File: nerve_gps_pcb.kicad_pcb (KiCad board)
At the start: 4 copper layers, 50 x 50 mm, 14 parts, among them J1 BF080-16-A-1-L-C, J2 WS2812B, J3 5V GPIO Breakout, U1 SAM-M10Q, U2 TXB0104QPWRQ1

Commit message: Update config.kibot.yaml, cleanup, add fiducials
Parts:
- added FM1: 1mm, Fiducial:Fiducial_1mm_Mask2mm, F.Cu at (129.8, 120.0)
- added FM2: 1mm, Fiducial:Fiducial_1mm_Mask2mm, F.Cu at (129.8, 90.0)
- added FM3: 1mm, Fiducial:Fiducial_1mm_Mask2mm, F.Cu at (167.2, 90.0)
- added FM4: 1mm, Fiducial:Fiducial_1mm_Mask2mm, B.Cu at (129.8, 120.0)
- added FM5: 1mm, Fiducial:Fiducial_1mm_Mask2mm, B.Cu at (129.8, 90.0)
- added FM6: 1mm, Fiducial:Fiducial_1mm_Mask2mm, B.Cu at (167.2, 90.0)
- turned H2 to 135 degrees
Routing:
- net Net-(D4-DOUT): track 14.9 -> 16.3 mm

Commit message: Major cleanup and update component_library
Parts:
- U2: moved to B.Cu
- moved J3 20.5 mm to (171.0, 102.5), turned to 180 degrees
- moved J2 11.9 mm to (159.7, 89.5), turned to 90 degrees
- moved U2 7.98 mm to (161.5, 105.0)
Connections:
- net +3.3VBATT renamed +3VBATT
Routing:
- net /GPIO_3_{5V}: track 28.7 -> 13.2 mm
- net +3V3: track 38.8 -> 25.5 mm, vias 10 -> 4
- net /GPIO_2_{5V}: track 24.5 -> 11.5 mm
- net /GPIO_1_{5V}: track 20.3 -> 9.66 mm
- net Net-(D4-DOUT): track 16.3 -> 8.76 mm
- net GND: track 45.1 -> 41.0 mm, vias 92 -> 111
- net /GPIO_3: track 12.5 -> 9.01 mm, vias 1 -> 0
- net /GPIO_2: track 10.1 -> 7.18 mm, vias 1 -> 0
- net /GPIO_1: track 6.47 -> 5.49 mm, vias 1 -> 0
- net /GPS_UART_RX: track 20.4 -> 19.5 mm
- net +3VBATT: track 52.5 -> 51.8 mm
- net /GPS_UART_TX: track 20.2 -> 19.5 mm
- net +5V: track 12.7 -> 13.1 mm, vias 5 -> 8
- added copper zone on F.Cu, net +5V
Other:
- board text added: "5V"
- board text added: "CR1220 3V"
- board text added: "GND"
- board text added: "GPIO1_{5V}"
- board text added: "GPIO2_{5V}"
- board text added: "GPIO3_{5V}"
- board text added: "PWM_{RGB}"

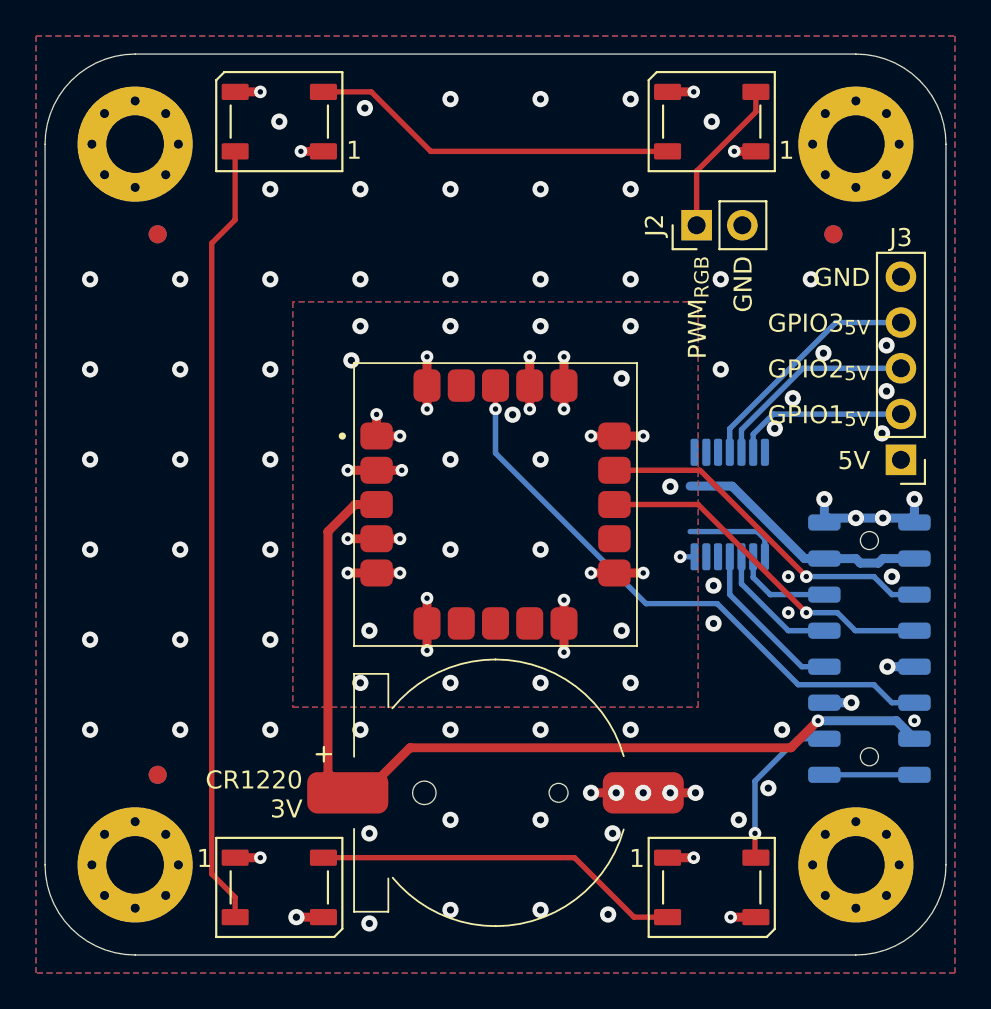
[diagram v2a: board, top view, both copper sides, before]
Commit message: Cleanup silkscreen
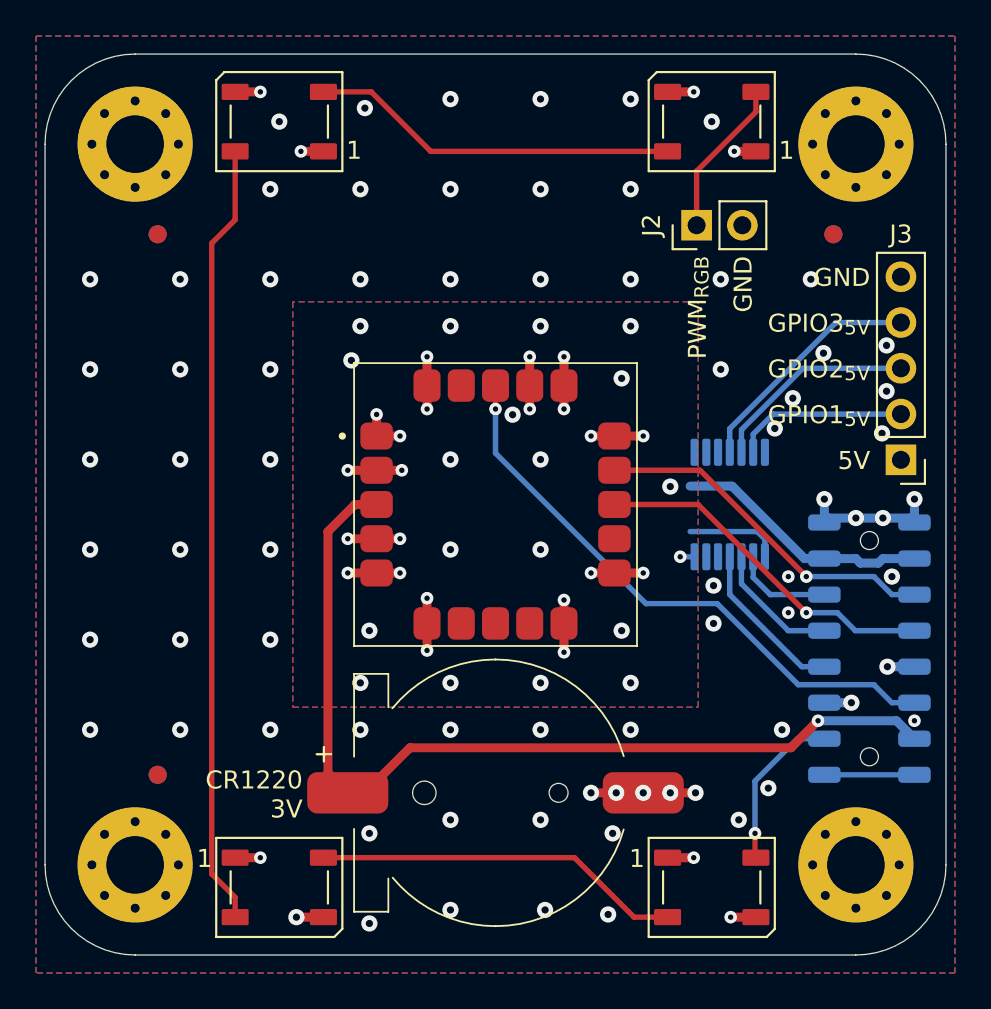
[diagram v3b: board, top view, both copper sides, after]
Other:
- board text added: "Daniel Jeon nerve_gps_pcb v0.1.0-alpha"
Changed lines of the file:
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@@
 		(tags "Through hole pin header THT 1x02 2.54mm single row")
 		(property "Reference" "J2"
-			(at 0 -2.33 90)
+			(at 0 -2.5 90)
 			(layer "F.SilkS")
 			(effects
@@
 		(tags "Through hole pin header THT 1x05 2.54mm single row")
 		(property "Reference" "J3"
-			(at 0 12.325 180)
+			(at 0 12.52 180)
 			(layer "F.SilkS")
 			(effects
@@
 				(font
 					(size 1 1)
-					(thickness 0.1)
+					(thickness 0.15)
 				)
 				(justify mirror)
@@
 		)
 	)
+	(gr_text "Daniel Jeon\nnerve_gps_pcb\nv0.1.0-alpha"
+		(at 148.5 128.75 0)
+		(layer "B.SilkS")
+		(effects
+			(font
+				(size 1 1)
+				(thickness 0.2)
+				(bold yes)
+			)
+			(justify bottom mirror)
+		)
+	)
 	(gr_text "GPIO3_{5V}"
 		(at 169.32619 95.53 0)
@@
 	)
 	(via
-		(at 151 127.5)
+		(at 151.25 127.5)
 		(size 0.9)
 		(drill 0.4)

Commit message: Fix #2
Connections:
- U1 pad 13: /GPS_UART_RX -> /GPS_UART_TX
- U1 pad 14: /GPS_UART_TX -> /GPS_UART_RX
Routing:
- net /GPS_UART_RX: track 19.5 -> 20.3 mm
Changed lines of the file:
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@@
 			(layers "F.Cu" "F.Mask")
 			(roundrect_rratio 0.25)
-			(net 11 "/GPS_UART_RX")
+			(net 8 "/GPS_UART_TX")
 			(pinfunction "TXD")
 			(pintype "output")
@@
 			(layers "F.Cu" "F.Mask")
 			(roundrect_rratio 0.25)
-			(net 8 "/GPS_UART_TX")
+			(net 11 "/GPS_UART_RX")
 			(pinfunction "RXD")
 			(pintype "input")
@@
 	)
 	(via
-		(at 164.75 109)
+		(at 164.849997 109)
 		(size 0.7)
 		(drill 0.3)
@@
 	)
 	(via
-		(at 158.200216 104.001988)
+		(at 157 104.001988)
 		(size 0.9)
 		(drill 0.4)
@@
 	)
 	(segment
-		(start 165.75 109)
-		(end 159.85 103.1)
+		(start 165.75 111)
+		(end 159.75 105)
 		(width 0.3)
 		(layer "F.Cu")
@@
 	)
 	(segment
-		(start 159.85 103.1)
-		(end 155.1 103.1)
+		(start 169.25 111)
+		(end 165.75 111)
+		(width 0.3)
+		(layer "F.Cu")
+		(net 8)
+	)
+	(segment
+		(start 170.25 110)
+		(end 169.25 111)
+		(width 0.3)
+		(layer "F.Cu")
+		(net 8)
+	)
+	(segment
+		(start 159.75 105)
+		(end 155.1 105)
 		(width 0.3)
 		(layer "F.Cu")
@@
 	)
 	(via
-		(at 165.75 109)
+		(at 170.25 110)
 		(size 0.7)
 		(drill 0.3)
@@
 	)
 	(segment
-		(start 169.5 109)
-		(end 170.5 110)
-		(width 0.3)
-		(layer "B.Cu")
-		(net 8)
-	)
-	(segment
-		(start 165.75 109)
-		(end 169.5 109)
-		(width 0.3)
-		(layer "B.Cu")
-		(net 8)
-	)
-	(segment
-		(start 170.5 110)
+		(start 170.25 110)
 		(end 171.75 110)
 		(width 0.3)
@@
 	)
 	(segment
-		(start 159.75 105)
-		(end 155.1 105)
+		(start 159.85 103.1)
+		(end 155.1 103.1)
 		(width 0.3)
 		(layer "F.Cu")
@@
 	)
 	(segment
-		(start 165.75 111)
-		(end 159.75 105)
+		(start 165.75 109)
+		(end 159.85 103.1)
 		(width 0.3)
 		(layer "F.Cu")
@@
 	)
 	(via
-		(at 165.75 111)
+		(at 165.75 109)
 		(size 0.7)
 		(drill 0.3)
@@
 	)
 	(segment
-		(start 165.75 111)
-		(end 167.469408 111)
+		(start 170.469408 112)
+		(end 171.75 112)
 		(width 0.3)
 		(layer "B.Cu")
@@
 	)
 	(segment
-		(start 168.469408 112)
-		(end 171.75 112)
+		(start 167.469408 109)
+		(end 170.469408 112)
 		(width 0.3)
 		(layer "B.Cu")
@@
 	)
 	(segment
-		(start 167.469408 111)
-		(end 168.469408 112)
+		(start 165.75 109)
+		(end 167.469408 109)
 		(width 0.3)
 		(layer "B.Cu")

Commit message: Update versioning and docs pictures
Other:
- board text added: "Daniel Jeon nerve_gps_pcb v0.1.0"
- board text removed: "Daniel Jeon nerve_gps_pcb v0.1.0-alpha"
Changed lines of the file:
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@@
 	(title_block
 		(title "Nerve GPS PCB")
-		(rev "0.1.0-alpha")
+		(rev "0.1.0")
 	)
 	(layers
@@
 		)
 	)
-	(gr_text "Daniel Jeon\nnerve_gps_pcb\nv0.1.0-alpha"
+	(gr_text "Daniel Jeon\nnerve_gps_pcb\nv0.1.0"
 		(at 148.5 128.75 0)
 		(layer "B.SilkS")

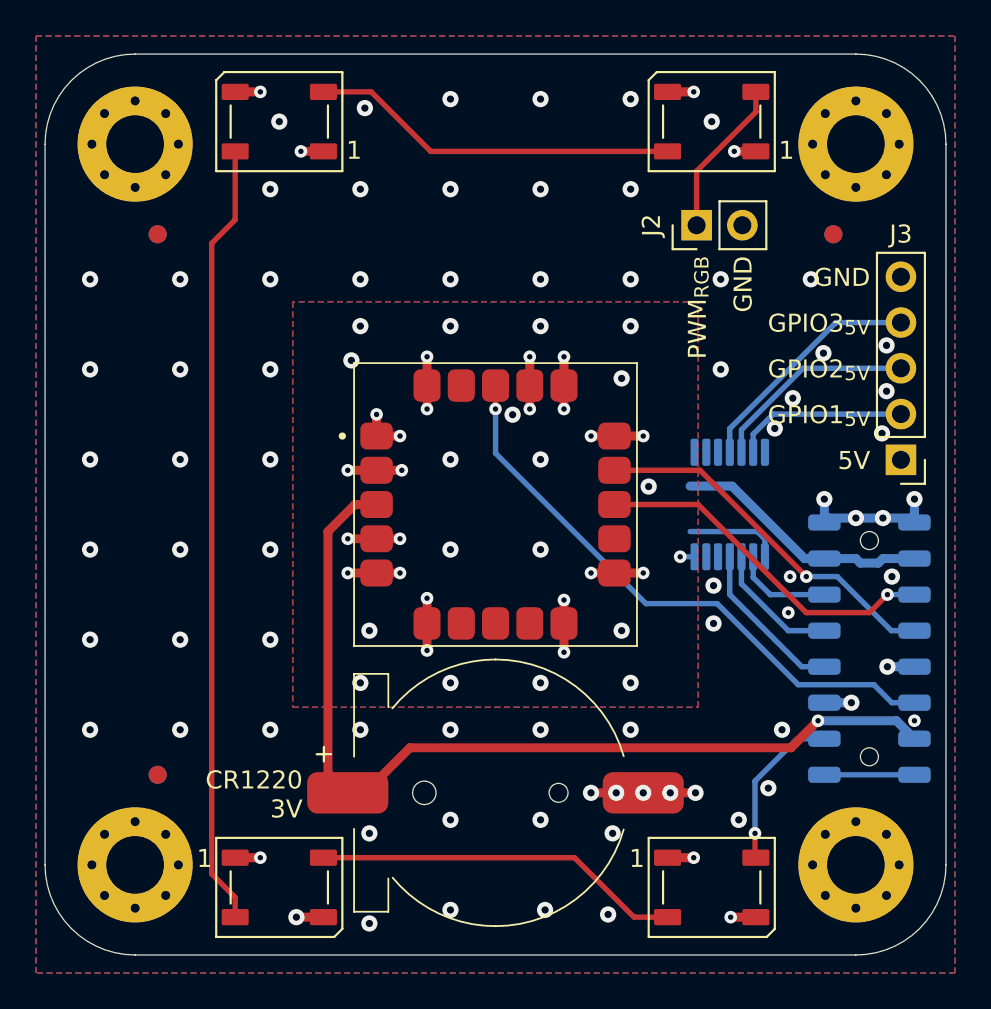
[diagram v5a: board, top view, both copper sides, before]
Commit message: Update for KiCad 9.0 and component library
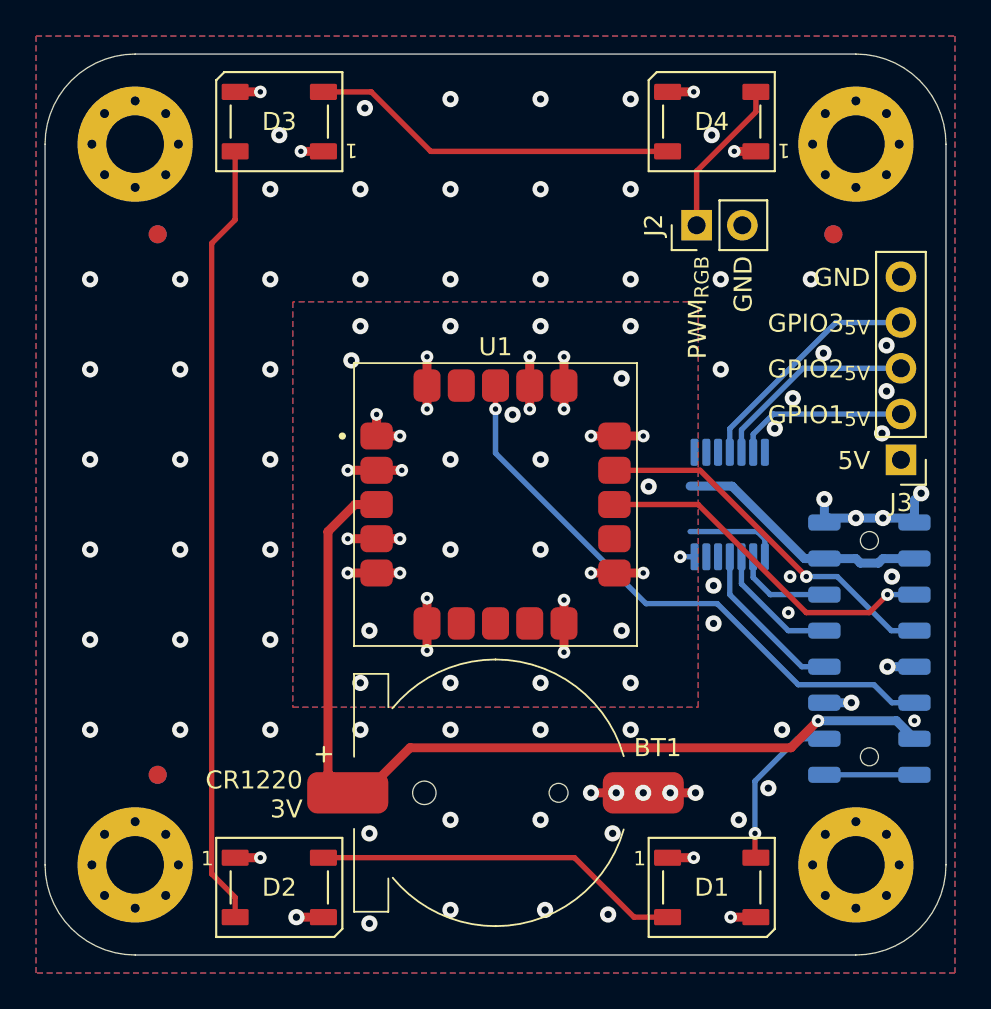
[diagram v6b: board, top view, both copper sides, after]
